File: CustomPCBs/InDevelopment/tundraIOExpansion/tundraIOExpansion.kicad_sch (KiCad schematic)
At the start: 74 parts, among them J1 Conn_01x25, T1 BSS138BKS_115, T2 BSS138BKS_115, T3 BSS138BKS_115, T4 BSS138BKS_115, T5 BSS138BKS_115, U1 RP2040, U2 W25Q32JVSS, U3 HE6206-18NR, U4 W25Q32JVSS, U5 RP2040, Y1 12.000MHz, Y2 12.000MHz

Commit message: Schematic of new board looks complete for now
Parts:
- added R27, R28, R29, R30, R31, R33: 10k, Resistor_SMD:R_0201_0603Metric, symbol Device:R
- added T6, T7: BSS138BKS_115, footprints:SOT363, symbol BSS138BKS_115:BSS138BKS_115
- added U6: MOUDLE-SEEEDUINO-XIAO-ESP32C3, footprints:MOUDLE14P-SMD-2.54-21X17.8MM, symbol MOUDLE-SEEEDUINO-XIAO-ESP32C3:MOUDLE-SEEEDUINO-XIAO-ESP32C3
- J1: footprint my_connectors:25PIN FRONT FLIP 0.6mm PITCH AYF332535A -> footprints:25PIN FRONT FLIP 0.6mm PITCH AYF332535A
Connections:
- net +1V8: now also R29.1, R30.1, R33.1, T6.2, T6.5, T7.2
- net +3.3V: now also R27.1, R28.1, R31.1, U6.12 (3V3)
- net D10-MI_CS: no longer U1.16 (GPIO13)
- net D11-MI_MOSI: no longer U1.15 (GPIO12)
- net D12-MI_MISO: no longer U1.18 (GPIO15)
- net D13-MI_SCLK: no longer U1.17 (GPIO14)
- net GND: now also U6.13 (GND)
- net SCL1_3V3: now also U1.3 (GPIO1)
- net SCL2_3V3: now also U1.5 (GPIO3)
- net SCL3_3V3: now also U5.3 (GPIO1)
- net SCL4_3V3: now also U5.5 (GPIO3)
- net SCL5_3V3: now also U6.6 (PA9_A5_D5_SCL)
- net SDA1_3V3: now also U1.2 (GPIO0)
- net SDA2_3V3: now also U1.4 (GPIO2)
- net SDA3_3V3: now also U5.2 (GPIO0)
- net SDA4_3V3: now also U5.4 (GPIO2)
- net SDA5_3V3: now also U6.5 (PA8_A4_D4_SDA)
- net INTER_RP2040_ESP32_UART_TX0: now reaches U5.15 (GPIO12)
- net INTER_RP2040_ESP32_UART_TX0: now also U6.8 (PB09_A7_D7_RX)
- net INTER_RP2040_ESP32_UART_RX0: now reaches U5.16 (GPIO13)
- net INTER_RP2040_ESP32_UART_RX0: now also U6.7 (PB08_A6_D6_TX)
- new net SCK_1V8: R33.2, T7.1
- new net SCK_3V3: R31.2, T7.6, U6.9 (PA7_A8_D8_SCK)
- new net SDI_1V8: R30.2, T6.4
- new net SDI_3V3: R28.2, T6.3, U6.10 (PA5_A9_D9_MISO)
- new net SDO_1V8: R29.2, T6.1
- new net SDO_3V3: R27.2, T6.6, U6.11 (PA6_A10_D10_MOSI)
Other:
- moved on the sheet: C13, C14, FINGER1, FINGER2, FINGER3, FINGER4, FINGER5L1, FINGER5R1, R11, R12, R13, R14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

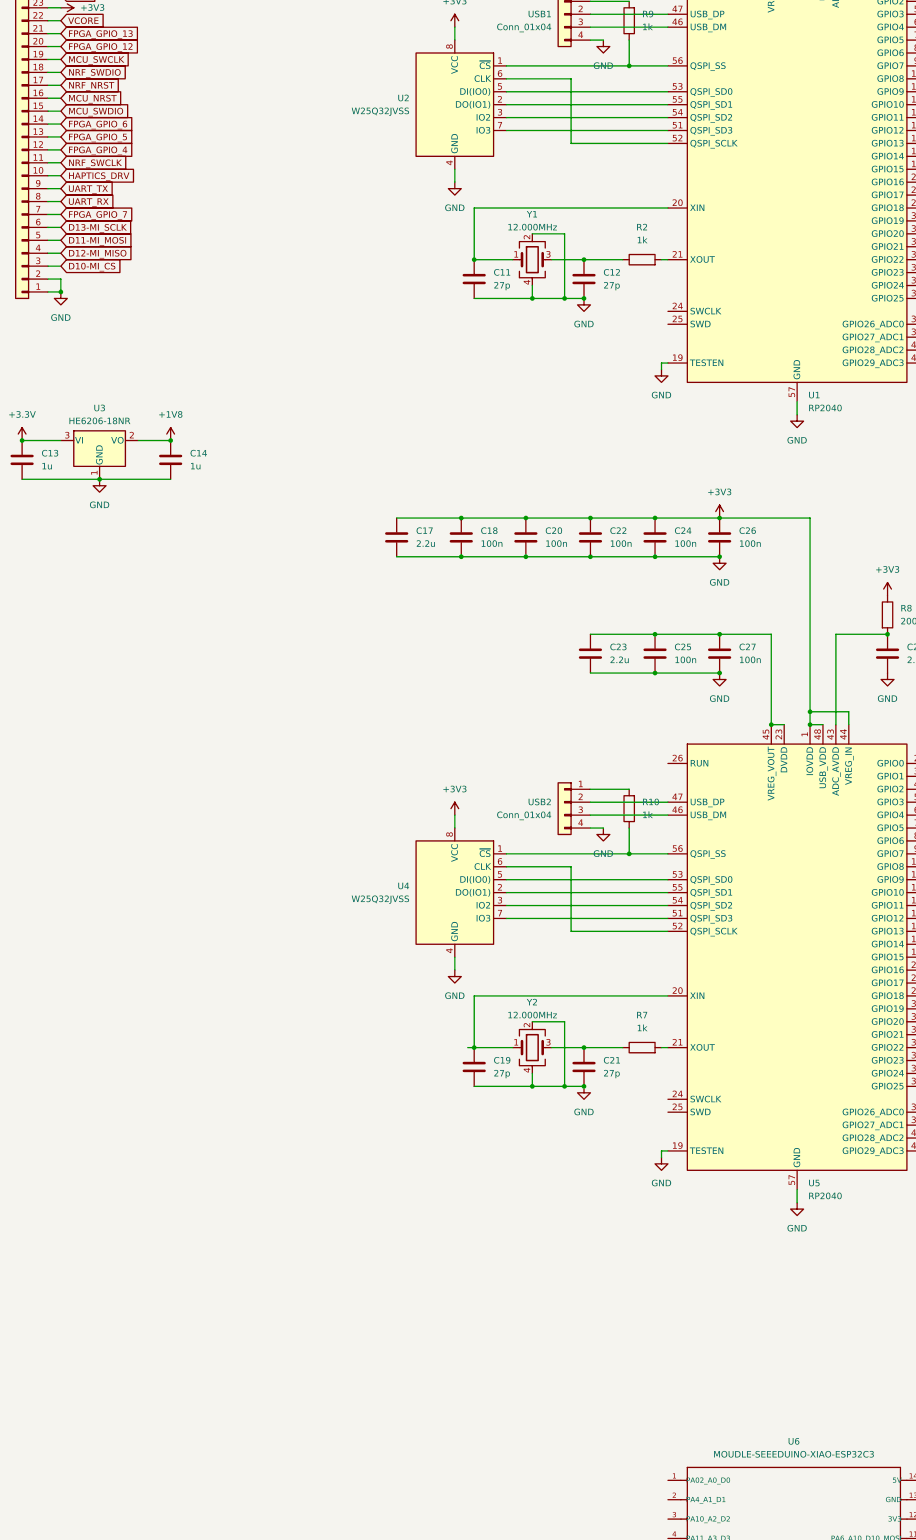
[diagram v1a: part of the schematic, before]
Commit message: Adding JLCPCB refs and choosing JLCPCB crystals
Adjusting cap values too, since the load capacitance also changes a bit
on the crystal I chose.
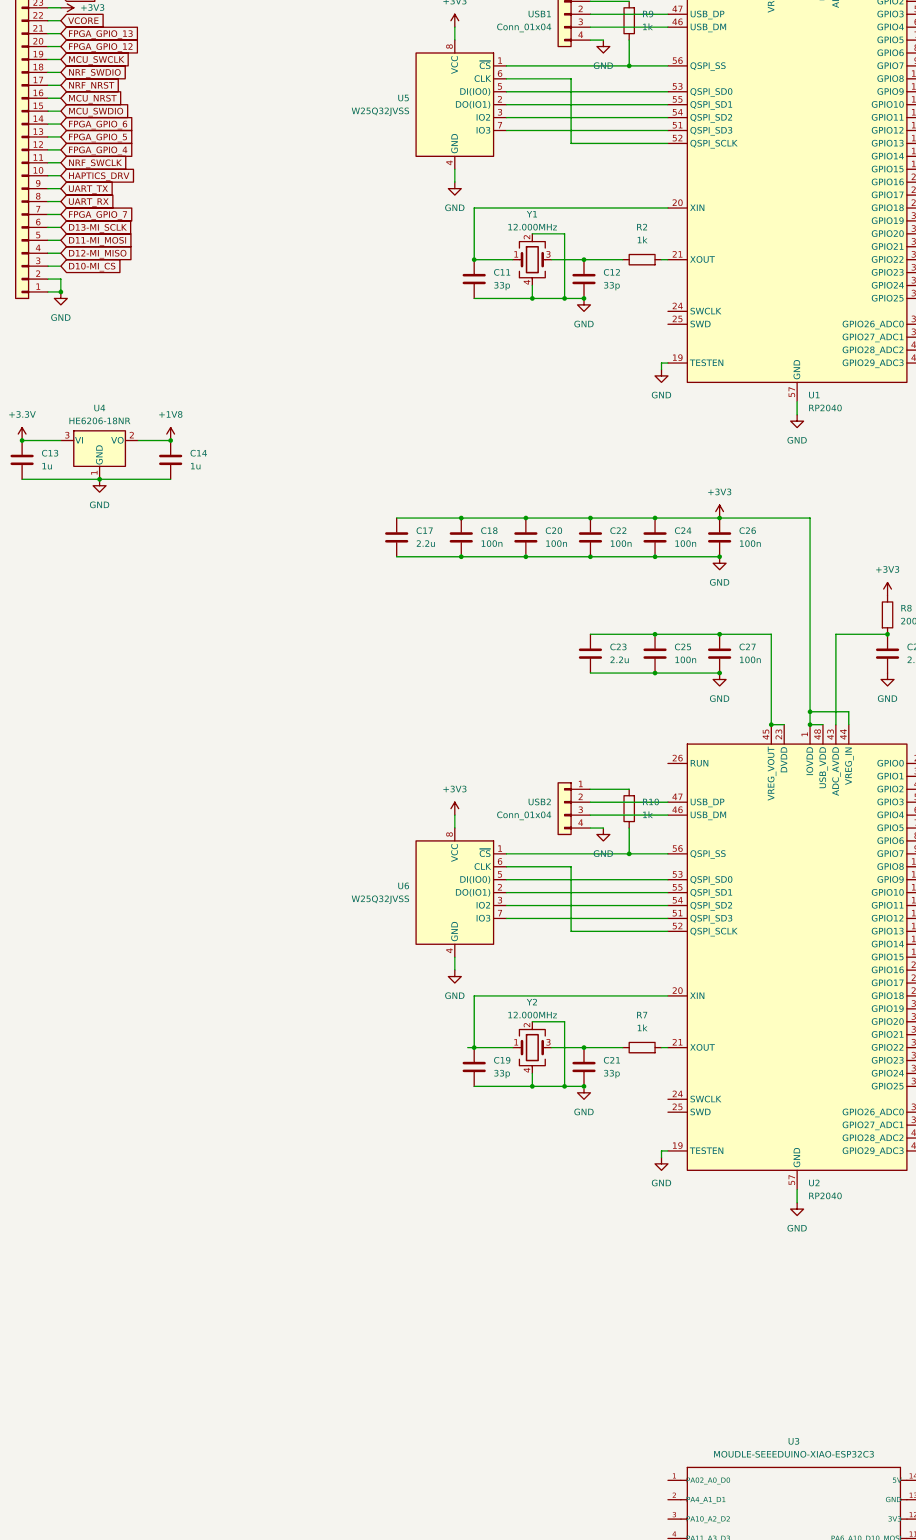
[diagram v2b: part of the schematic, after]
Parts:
- removed U2, U4: W25Q32JVSS, Package_SO:SOIC-8_5.23x5.23mm_P1.27mm, symbol Memory_Flash:W25Q32JVSS
- removed U3: HE6206-18NR, Package_TO_SOT_SMD:SOT-23-3, symbol Regulator_Linear:XC6206PxxxMR
- removed U5: RP2040, Package_DFN_QFN:QFN-56-1EP_7x7mm_P0.4mm_EP3.2x3.2mm, symbol MCU_RaspberryPi:RP2040
- removed U6: MOUDLE-SEEEDUINO-XIAO-ESP32C3, footprints:MOUDLE14P-SMD-2.54-21X17.8MM, symbol MOUDLE-SEEEDUINO-XIAO-ESP32C3:MOUDLE-SEEEDUINO-XIAO-ESP32C3
- added U2: RP2040, Package_DFN_QFN:QFN-56-1EP_7x7mm_P0.4mm_EP3.2x3.2mm, symbol MCU_RaspberryPi:RP2040
- added U3: MOUDLE-SEEEDUINO-XIAO-ESP32C3, footprints:MOUDLE14P-SMD-2.54-21X17.8MM, symbol MOUDLE-SEEEDUINO-XIAO-ESP32C3:MOUDLE-SEEEDUINO-XIAO-ESP32C3
- added U4: HE6206-18NR, Package_TO_SOT_SMD:SOT-23-3, symbol Regulator_Linear:XC6206PxxxMR
- added U5, U6: W25Q32JVSS, Package_SO:SOIC-8_5.23x5.23mm_P1.27mm, symbol Memory_Flash:W25Q32JVSS
- C11, C12, C19, C21: value 27p -> 33p
- U1: JLCPCB (none) -> https://jlcpcb.com/partdetail/RaspberryPi-RP2040/C2040
- Y1, Y2: footprint Crystal:Crystal_SMD_3225-4Pin_3.2x2.5mm -> Crystal:Crystal_SMD_2520-4Pin_2.5x2.0mm; JLCPCB\ (none) -> https://jlcpcb.com/partdetail/3151532-SX2B12000F2010F30/C29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
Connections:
- net +1V8: now also U4.2 (VO)
- net +3.3V: now also U3.12 (3V3), U4.3 (VI)
- net +3V3: now also U2.1 (IOVDD), U2.10 (IOVDD), U2.22 (IOVDD), U2.33 (IOVDD), U2.42 (IOVDD), U2.44 (VREG_IN), U2.48 (USB_VDD), U2.49 (IOVDD), U5.8 (VCC), U6.8 (VCC)
- net GND: now also U2.19 (TESTEN), U2.57 (GND), U3.13 (GND), U4.1 (GND), U5.4 (GND), U6.4 (GND)
- net INTER_RP2040_ESP32_UART_RX0: now also U2.16 (GPIO13), U3.7 (PB08_A6_D6_TX)
- net INTER_RP2040_ESP32_UART_TX0: now also U2.15 (GPIO12), U3.8 (PB09_A7_D7_RX)
- net INTER_RP2040_UART_RX1: now also U2.6 (GPIO4)
- net INTER_RP2040_UART_TX1: now also U2.7 (GPIO5)
- net SCK_3V3: now also U3.9 (PA7_A8_D8_SCK)
- net SCL3_3V3: now also U2.3 (GPIO1)
- net SCL4_3V3: now also U2.5 (GPIO3)
- net SCL5_3V3: now also U3.6 (PA9_A5_D5_SCL)
- net SDA3_3V3: now also U2.2 (GPIO0)
- net SDA4_3V3: now also U2.4 (GPIO2)
- net SDA5_3V3: now also U3.5 (PA8_A4_D4_SDA)
- net SDI_3V3: now also U3.10 (PA5_A9_D9_MISO)
- net SDO_3V3: now also U3.11 (PA6_A10_D10_MOSI)
- net at R9.1, U1.56 (QSPI_SS): now also U5.1 (~{CS})
- net at U1.55 (QSPI_SD1): now also U5.2 (DO(IO1))
- net at U1.54 (QSPI_SD2): now also U5.3 (IO2)
- net at U1.53 (QSPI_SD0): now also U5.5 (DI(IO0))
- net at U1.52 (QSPI_SCLK): now also U5.6 (CLK)
- net at U1.51 (QSPI_SD3): now also U5.7 (IO3)
- net at C23.1, C25.1, C27.1: now also U2.23 (DVDD), U2.45 (VREG_VOUT), U2.50 (DVDD)
- net at R7.2: now also U2.21 (XOUT)
- net at C19.1, Y2.1: now also U2.20 (XIN)
- net at R10.1: now also U2.56 (QSPI_SS), U6.1 (~{CS})
- net at C28.1, R8.2: now also U2.43 (ADC_AVDD)
- net at FingerAux1.1 (Pin_1): now also U2.34 (GPIO22)
- net at FingerAux1.2 (Pin_2): now also U2.35 (GPIO23)
- net at FingerAux1.3 (Pin_3): now also U2.36 (GPIO24)
- net at FingerAux1.4 (Pin_4): now also U2.37 (GPIO25)
- net at FingerAux1.5 (Pin_5): now also U2.38 (GPIO26_ADC0)
- net at FingerAux1.6 (Pin_6): now also U2.39 (GPIO27_ADC1)
- net at FingerAux1.7 (Pin_7): now also U2.40 (GPIO28_ADC2)
- net at FingerAux1.8 (Pin_8): now also U2.41 (GPIO29_ADC3)
- net at USB2.2 (Pin_2): now also U2.47 (USB_DP)
- net at USB2.3 (Pin_3): now also U2.46 (USB_DM)
- new net: U2.51 (QSPI_SD3), U6.7 (IO3)
- new net: U2.52 (QSPI_SCLK), U6.6 (CLK)
- new net: U2.53 (QSPI_SD0), U6.5 (DI(IO0))
- new net: U2.54 (QSPI_SD2), U6.3 (IO2)
- new net: U2.55 (QSPI_SD1), U6.2 (DO(IO1))

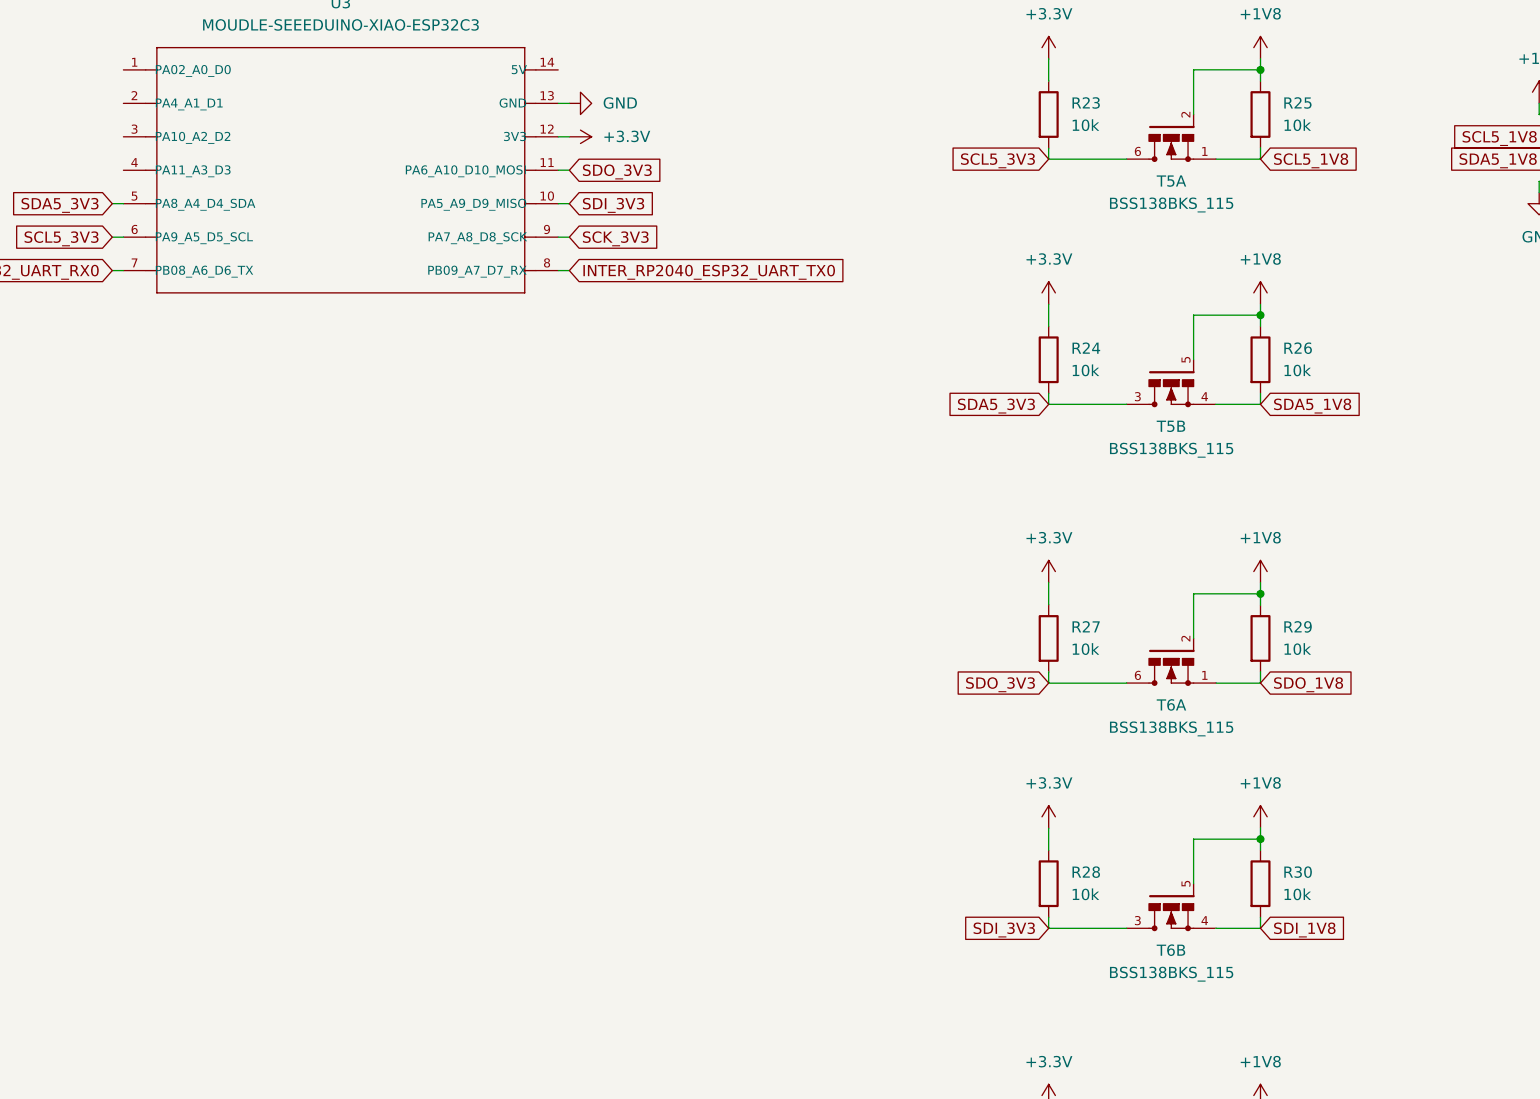
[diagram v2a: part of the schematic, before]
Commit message: New XIAO ESP32C3 TH footprint, ICM on main board
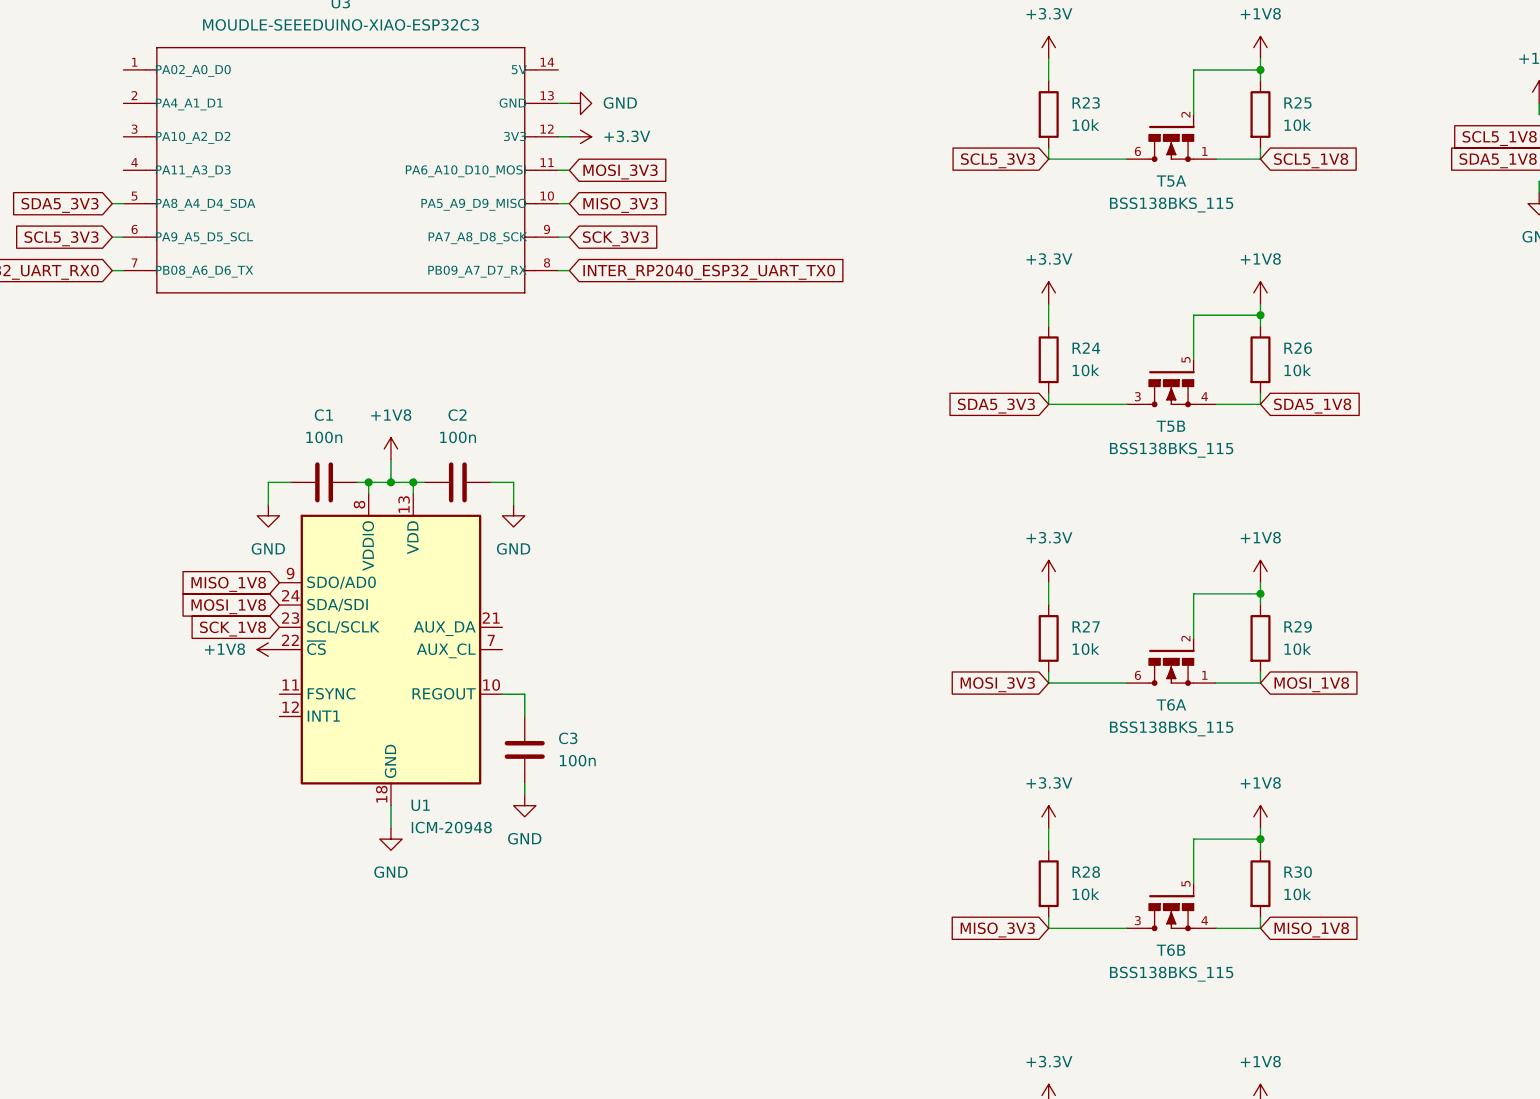
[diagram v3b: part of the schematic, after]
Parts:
- added C1, C2, C3: 100n, Capacitor_SMD:C_0201_0603Metric, symbol Device:C
- added U1: ICM-20948, Sensor_Motion:InvenSense_QFN-24_3x3mm_P0.4mm, symbol Sensor_Motion:ICM-20948
- U3: footprint footprints:MOUDLE14P-SMD-2.54-21X17.8MM -> footprints:MOUDLE14P-SMD-2.54-21X17.8MM_TH
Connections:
- net +1V8: now also C1.2, C2.1, U1.13 (VDD), U1.22 (~{CS}), U1.8 (VDDIO)
- net GND: now also C1.1, C2.2, C3.2, U1.18 (GND), U1.20 (GND)
- net SCK_1V8: now also U1.23 (SCL/SCLK)
- net SDI_1V8 renamed MISO_1V8
- net MISO_1V8: now also U1.9 (SDO/AD0)
- net SDI_3V3 renamed MISO_3V3
- net SDO_1V8 renamed MOSI_1V8
- net MOSI_1V8: now also U1.24 (SDA/SDI)
- net SDO_3V3 renamed MOSI_3V3
- new net: C3.1, U1.10 (REGOUT)

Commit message: Part positions more or less finished on main board
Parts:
- added R32, R34: 10k, Resistor_SMD:R_0201_0603Metric, symbol Device:R
- added unit 2 of T7
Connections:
- net +1V8: now also R34.1, T7.5; no longer U1.22 (~{CS})
- net +3.3V: now also R32.1
- net nCS_3V3: now reaches U3.4 (PA11_A3_D3)
- net nCS_3V3: now also R32.2, T7.3
- new net nCS_1V8: R34.2, T7.4, U1.22 (~{CS})
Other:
- moved on the sheet: C1, C2, C3, FINGER5L1, FINGER5R1, R23, R24, R25, R26, T5A, T5B, U1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
